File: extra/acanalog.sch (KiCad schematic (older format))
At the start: 20 parts, among them U1 TL074

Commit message: a lot more layout work
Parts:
- R10, R11, R12, R13, R14, R15, R16, R17, R18, R19, R20, R5, R6, R7, R8, R9: renamed from R?; footprint (none) -> xnorman:Resistor_Horizontal_RM10mm-xnorman
- gave numbers to parts that had none: 3
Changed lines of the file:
@@
 $EndDescr
 $Comp
-L CONN_01X03 P?
+L CONN_01X03 P7
 U 1 1 58575363
 P 1200 1350
-F 0 "P?" H 1200 1550 50  0000 C CNN
+F 0 "P7" H 1200 1550 50  0000 C CNN
 F 1 "CONN_01X03" V 1300 1350 50  0000 C CNN
-F 2 "" H 1200 1350 50  0000 C CNN
+F 2 "" H 1200 1350 50  0001 C CNN
 F 3 "" H 1200 1350 50  0000 C CNN
 	1    1200 1350
@@
 $EndComp
 $Comp
-L CONN_01X03 P?
+L CONN_01X03 P8
 U 1 1 5857536A
 P 5100 1250
-F 0 "P?" H 5100 1450 50  0000 C CNN
+F 0 "P8" H 5100 1450 50  0000 C CNN
 F 1 "CONN_01X03" V 5200 1250 50  0000 C CNN
-F 2 "" H 5100 1250 50  0000 C CNN
+F 2 "" H 5100 1250 50  0001 C CNN
 F 3 "" H 5100 1250 50  0000 C CNN
 	1    5100 1250
@@
 F 0 "U1" H 3000 2150 50  0000 C CNN
 F 1 "TL074" H 3100 1750 50  0000 C CNN
-F 2 "" H 2900 2050 50  0000 C CNN
+F 2 "" H 2900 2050 50  0001 C CNN
 F 3 "" H 3000 2150 50  0000 C CNN
 	1    2950 1950
@@
 $EndComp
 $Comp
-L R R?
+L R R5
 U 1 1 58575378
 P 2000 2050
-F 0 "R?" V 2080 2050 50  0000 C CNN
+F 0 "R5" V 2080 2050 50  0000 C CNN
 F 1 "2k" V 2000 2050 50  0000 C CNN
-F 2 "" V 1930 2050 50  0000 C CNN
+F 2 "xnorman:Resistor_Horizontal_RM10mm-xnorman" V 1930 2050 50  0001 C CNN
 F 3 "" H 2000 2050 50  0000 C CNN
 	1    2000 2050
@@
 $EndComp
 $Comp
-L R R?
+L R R9
 U 1 1 5857537F
 P 3050 2600
-F 0 "R?" V 3130 2600 50  0000 C CNN
+F 0 "R9" V 3130 2600 50  0000 C CNN
 F 1 "10k" V 3050 2600 50  0000 C CNN
-F 2 "" V 2980 2600 50  0000 C CNN
+F 2 "xnorman:Resistor_Horizontal_RM10mm-xnorman" V 2980 2600 50  0001 C CNN
 F 3 "" H 3050 2600 50  0000 C CNN
 	1    3050 2600
@@
 Connection ~ 2300 2050
 $Comp
-L GND #PWR?
+L GND #PWR08
 U 1 1 5857538D
 P 2450 1750
-F 0 "#PWR?" H 2450 1500 50  0001 C CNN
+F 0 "#PWR08" H 2450 1500 50  0001 C CNN
 F 1 "GND" H 2450 1600 50  0000 C CNN
 F 2 "" H 2450 1750 50  0000 C CNN
@@
 Connection ~ 3450 1950
 $Comp
-L R R?
+L R R13
 U 1 1 5857539F
 P 3700 1950
-F 0 "R?" V 3780 1950 50  0000 C CNN
+F 0 "R13" V 3780 1950 50  0000 C CNN
 F 1 "1k" V 3700 1950 50  0000 C CNN
-F 2 "" V 3630 1950 50  0000 C CNN
+F 2 "xnorman:Resistor_Horizontal_RM10mm-xnorman" V 3630 1950 50  0001 C CNN
 F 3 "" H 3700 1950 50  0000 C CNN
 	1    3700 1950
@@
 F 0 "U1" H 3000 3500 50  0000 C CNN
 F 1 "TL074" H 3100 3100 50  0000 C CNN
-F 2 "" H 2900 3400 50  0000 C CNN
+F 2 "" H 2900 3400 50  0001 C CNN
 F 3 "" H 3000 3500 50  0000 C CNN
 	2    2950 3300
@@
 $EndComp
 $Comp
-L R R?
+L R R6
 U 1 1 585753AE
 P 2000 3400
-F 0 "R?" V 2080 3400 50  0000 C CNN
+F 0 "R6" V 2080 3400 50  0000 C CNN
 F 1 "2k" V 2000 3400 50  0000 C CNN
-F 2 "" V 1930 3400 50  0000 C CNN
+F 2 "xnorman:Resistor_Horizontal_RM10mm-xnorman" V 1930 3400 50  0001 C CNN
 F 3 "" H 2000 3400 50  0000 C CNN
 	1    2000 3400
@@
 $EndComp
 $Comp
-L R R?
+L R R10
 U 1 1 585753B5
 P 3050 3950
-F 0 "R?" V 3130 3950 50  0000 C CNN
+F 0 "R10" V 3130 3950 50  0000 C CNN
 F 1 "10k" V 3050 3950 50  0000 C CNN
-F 2 "" V 2980 3950 50  0000 C CNN
+F 2 "xnorman:Resistor_Horizontal_RM10mm-xnorman" V 2980 3950 50  0001 C CNN
 F 3 "" H 3050 3950 50  0000 C CNN
 	1    3050 3950
@@
 Connection ~ 2300 3400
 $Comp
-L GND #PWR?
+L GND #PWR09
 U 1 1 585753C3
 P 2450 3100
-F 0 "#PWR?" H 2450 2850 50  0001 C CNN
+F 0 "#PWR09" H 2450 2850 50  0001 C CNN
 F 1 "GND" H 2450 2950 50  0000 C CNN
 F 2 "" H 2450 3100 50  0000 C CNN
@@
 Connection ~ 3450 3300
 $Comp
-L R R?
+L R R14
 U 1 1 585753D5
 P 3700 3300
-F 0 "R?" V 3780 3300 50  0000 C CNN
+F 0 "R14" V 3780 3300 50  0000 C CNN
 F 1 "1k" V 3700 3300 50  0000 C CNN
-F 2 "" V 3630 3300 50  0000 C CNN
+F 2 "xnorman:Resistor_Horizontal_RM10mm-xnorman" V 3630 3300 50  0001 C CNN
 F 3 "" H 3700 3300 50  0000 C CNN
 	1    3700 3300
@@
 F 0 "U1" H 3000 4950 50  0000 C CNN
 F 1 "TL074" H 3100 4550 50  0000 C CNN
-F 2 "" H 2900 4850 50  0000 C CNN
+F 2 "" H 2900 4850 50  0001 C CNN
 F 3 "" H 3000 4950 50  0000 C CNN
 	4    2950 4750
@@
 $EndComp
 $Comp
-L R R?
+L R R7
 U 1 1 585753E4
 P 2000 4850
-F 0 "R?" V 2080 4850 50  0000 C CNN
+F 0 "R7" V 2080 4850 50  0000 C CNN
 F 1 "100k" V 2000 4850 50  0000 C CNN
-F 2 "" V 1930 4850 50  0000 C CNN
+F 2 "xnorman:Resistor_Horizontal_RM10mm-xnorman" V 1930 4850 50  0001 C CNN
 F 3 "" H 2000 4850 50  0000 C CNN
 	1    2000 4850
@@
 $EndComp
 $Comp
-L R R?
+L R R11
 U 1 1 585753EB
 P 3050 5400
-F 0 "R?" V 3130 5400 50  0000 C CNN
+F 0 "R11" V 3130 5400 50  0000 C CNN
 F 1 "100k" V 3050 5400 50  0000 C CNN
-F 2 "" V 2980 5400 50  0000 C CNN
+F 2 "xnorman:Resistor_Horizontal_RM10mm-xnorman" V 2980 5400 50  0001 C CNN
 F 3 "" H 3050 5400 50  0000 C CNN
 	1    3050 5400
@@
 Connection ~ 2300 4850
 $Comp
-L GND #PWR?
+L GND #PWR010
 U 1 1 585753F9
 P 2450 4550
-F 0 "#PWR?" H 2450 4300 50  0001 C CNN
+F 0 "#PWR010" H 2450 4300 50  0001 C CNN
 F 1 "GND" H 2450 4400 50  0000 C CNN
 F 2 "" H 2450 4550 50  0000 C CNN
@@
 Connection ~ 3450 4750
 $Comp
-L R R?
+L R R15
 U 1 1 5857540B
 P 3700 4750
-F 0 "R?" V 3780 4750 50  0000 C CNN
+F 0 "R15" V 3780 4750 50  0000 C CNN
 F 1 "2k" V 3700 4750 50  0000 C CNN
-F 2 "" V 3630 4750 50  0000 C CNN
+F 2 "xnorman:Resistor_Horizontal_RM10mm-xnorman" V 3630 4750 50  0001 C CNN
 F 3 "" H 3700 4750 50  0000 C CNN
 	1    3700 4750
@@
 $EndComp
 $Comp
-L R R?
+L R R17
 U 1 1 58575412
 P 4100 4750
-F 0 "R?" V 4180 4750 50  0000 C CNN
+F 0 "R17" V 4180 4750 50  0000 C CNN
 F 1 "2k" V 4100 4750 50  0000 C CNN
-F 2 "" V 4030 4750 50  0000 C CNN
+F 2 "xnorman:Resistor_Horizontal_RM10mm-xnorman" V 4030 4750 50  0001 C CNN
 F 3 "" H 4100 4750 50  0000 C CNN
 	1    4100 4750
@@
 $EndComp
 $Comp
-L R R?
+L R R19
 U 1 1 58575419
 P 4400 5000
-F 0 "R?" V 4480 5000 50  0000 C CNN
+F 0 "R19" V 4480 5000 50  0000 C CNN
 F 1 "1k" V 4400 5000 50  0000 C CNN
-F 2 "" V 4330 5000 50  0000 C CNN
+F 2 "xnorman:Resistor_Horizontal_RM10mm-xnorman" V 4330 5000 50  0001 C CNN
 F 3 "" H 4400 5000 50  0000 C CNN
 	1    4400 5000
@@
 Connection ~ 4400 4750
 $Comp
-L GND #PWR?
+L GND #PWR011
 U 1 1 58575424
 P 4400 5300
-F 0 "#PWR?" H 4400 5050 50  0001 C CNN
+F 0 "#PWR011" H 4400 5050 50  0001 C CNN
 F 1 "GND" H 4400 5150 50  0000 C CNN
 F 2 "" H 4400 5300 50  0000 C CNN
@@
 F 0 "U1" H 3000 6300 50  0000 C CNN
 F 1 "TL074" H 3100 5900 50  0000 C CNN
-F 2 "" H 2900 6200 50  0000 C CNN
+F 2 "" H 2900 6200 50  0001 C CNN
 F 3 "" H 3000 6300 50  0000 C CNN
 	3    2950 6100
@@
 $EndComp
 $Comp
-L R R?
+L R R8
 U 1 1 58575432
 P 2000 6200
-F 0 "R?" V 2080 6200 50  0000 C CNN
+F 0 "R8" V 2080 6200 50  0000 C CNN
 F 1 "100k" V 2000 6200 50  0000 C CNN
-F 2 "" V 1930 6200 50  0000 C CNN
+F 2 "xnorman:Resistor_Horizontal_RM10mm-xnorman" V 1930 6200 50  0001 C CNN
 F 3 "" H 2000 6200 50  0000 C CNN
 	1    2000 6200
@@
 $EndComp
 $Comp
-L R R?
+L R R12
 U 1 1 58575439
 P 3050 6750
-F 0 "R?" V 3130 6750 50  0000 C CNN
+F 0 "R12" V 3130 6750 50  0000 C CNN
 F 1 "100k" V 3050 6750 50  0000 C CNN
-F 2 "" V 2980 6750 50  0000 C CNN
+F 2 "xnorman:Resistor_Horizontal_RM10mm-xnorman" V 2980 6750 50  0001 C CNN
 F 3 "" H 3050 6750 50  0000 C CNN
 	1    3050 6750
@@
 Connection ~ 2300 6200
 $Comp
-L GND #PWR?
+L GND #PWR012
 U 1 1 58575447
 P 2450 5900
-F 0 "#PWR?" H 2450 5650 50  0001 C CNN
+F 0 "#PWR012" H 2450 5650 50  0001 C CNN
 F 1 "GND" H 2450 5750 50  0000 C CNN
 F 2 "" H 2450 5900 50  0000 C CNN
@@
 Connection ~ 3450 6100
 $Comp
-L R R?
+L R R16
 U 1 1 58575459
 P 3700 6100
-F 0 "R?" V 3780 6100 50  0000 C CNN
+F 0 "R16" V 3780 6100 50  0000 C CNN
 F 1 "2k" V 3700 6100 50  0000 C CNN
-F 2 "" V 3630 6100 50  0000 C CNN
+F 2 "xnorman:Resistor_Horizontal_RM10mm-xnorman" V 3630 6100 50  0001 C CNN
 F 3 "" H 3700 6100 50  0000 C CNN
 	1    3700 6100
@@
 $EndComp
 $Comp
-L R R?
+L R R18
 U 1 1 58575460
 P 4100 6100
-F 0 "R?" V 4180 6100 50  0000 C CNN
+F 0 "R18" V 4180 6100 50  0000 C CNN
 F 1 "2k" V 4100 6100 50  0000 C CNN
-F 2 "" V 4030 6100 50  0000 C CNN
+F 2 "xnorman:Resistor_Horizontal_RM10mm-xnorman" V 4030 6100 50  0001 C CNN
 F 3 "" H 4100 6100 50  0000 C CNN
 	1    4100 6100
@@
 $EndComp
 $Comp
-L R R?
+L R R20
 U 1 1 58575467
 P 4400 6350
-F 0 "R?" V 4480 6350 50  0000 C CNN
+F 0 "R20" V 4480 6350 50  0000 C CNN
 F 1 "1k" V 4400 6350 50  0000 C CNN
-F 2 "" V 4330 6350 50  0000 C CNN
+F 2 "xnorman:Resistor_Horizontal_RM10mm-xnorman" V 4330 6350 50  0001 C CNN
 F 3 "" H 4400 6350 50  0000 C CNN
 	1    4400 6350
@@
 Connection ~ 4400 6100
 $Comp
-L GND #PWR?
+L GND #PWR013
 U 1 1 58575472
 P 4400 6650
-F 0 "#PWR?" H 4400 6400 50  0001 C CNN
+F 0 "#PWR013" H 4400 6400 50  0001 C CNN
 F 1 "GND" H 4400 6500 50  0000 C CNN
 F 2 "" H 4400 6650 50  0000 C CNN
@@
 	1450 1350 1400 1350
 $Comp
-L GND #PWR?
+L GND #PWR014
 U 1 1 58575BEC
 P 1550 1550
-F 0 "#PWR?" H 1550 1300 50  0001 C CNN
+F 0 "#PWR014" H 1550 1300 50  0001 C CNN
 F 1 "GND" H 1550 1400 50  0000 C CNN
 F 2 "" H 1550 1550 50  0000 C CNN
@@
 belaacin2
 $Comp
-L GND #PWR?
+L GND #PWR015
 U 1 1 58575F21
 P 4700 1450
-F 0 "#PWR?" H 4700 1200 50  0001 C CNN
+F 0 "#PWR015" H 4700 1200 50  0001 C CNN
 F 1 "GND" H 4700 1300 50  0000 C CNN
 F 2 "" H 4700 1450 50  0000 C CNN
@@
 	4700 1350 4700 1450
 $Comp
-L CONN_02X04 P?
+L CONN_02X04 P9
 U 1 1 585765EB
 P 6650 3100
-F 0 "P?" H 6650 3350 50  0000 C CNN
+F 0 "P9" H 6650 3350 50  0000 C CNN
 F 1 "mod_ac-io" H 6650 2850 50  0000 C CNN
-F 2 "" H 6650 1900 50  0000 C CNN
+F 2 "" H 6650 1900 50  0001 C CNN
 F 3 "" H 6650 1900 50  0000 C CNN
 	1    6650 3100
@@
 	6350 3350 6150 3350
 $Comp
-L GND #PWR?
+L GND #PWR016
 U 1 1 58576B81
 P 6900 3400
-F 0 "#PWR?" H 6900 3150 50  0001 C CNN
+F 0 "#PWR016" H 6900 3150 50  0001 C CNN
 F 1 "GND" H 6900 3250 50  0000 C CNN
 F 2 "" H 6900 3400 50  0000 C CNN

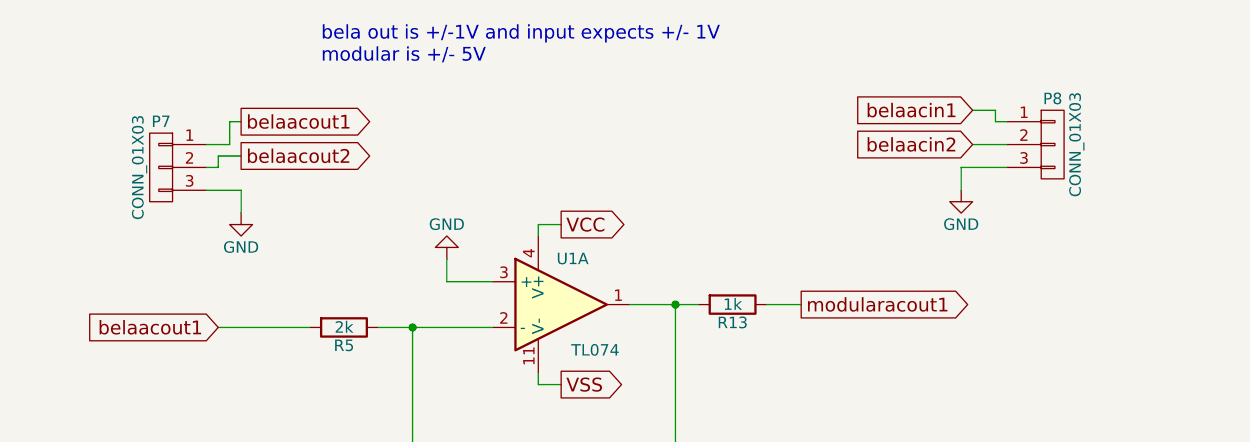
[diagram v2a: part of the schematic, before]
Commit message: starting pcb layout a little
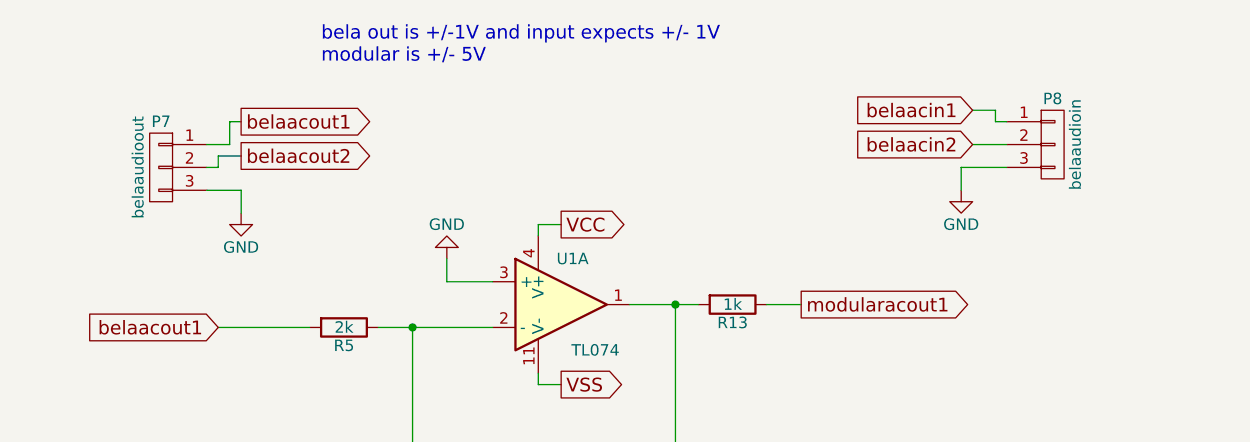
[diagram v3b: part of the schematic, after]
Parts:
- P7: value CONN_01X03 -> belaaudioout; footprint (none) -> Pin_Headers:Pin_Header_Straight_1x03_Pitch2.54mm
- P8: value CONN_01X03 -> belaaudioin; footprint (none) -> Pin_Headers:Pin_Header_Straight_1x03_Pitch2.54mm
- P9: footprint (none) -> Pin_Headers:Pin_Header_Straight_2x04_Pitch2.54mm
- U1: footprint (none) -> Housings_DIP:DIP-14_W7.62mm_LongPads
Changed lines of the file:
@@
 P 1200 1350
 F 0 "P7" H 1200 1550 50  0000 C CNN
-F 1 "CONN_01X03" V 1300 1350 50  0000 C CNN
-F 2 "" H 1200 1350 50  0001 C CNN
+F 1 "belaaudioout" V 1300 1350 50  0000 C CNN
+F 2 "Pin_Headers:Pin_Header_Straight_1x03_Pitch2.54mm" H 1200 1350 50  0001 C CNN
 F 3 "" H 1200 1350 50  0000 C CNN
 	1    1200 1350
@@
 P 5100 1250
 F 0 "P8" H 5100 1450 50  0000 C CNN
-F 1 "CONN_01X03" V 5200 1250 50  0000 C CNN
-F 2 "" H 5100 1250 50  0001 C CNN
+F 1 "belaaudioin" V 5200 1250 50  0000 C CNN
+F 2 "Pin_Headers:Pin_Header_Straight_1x03_Pitch2.54mm" H 5100 1250 50  0001 C CNN
 F 3 "" H 5100 1250 50  0000 C CNN
 	1    5100 1250
@@
 F 0 "U1" H 3000 2150 50  0000 C CNN
 F 1 "TL074" H 3100 1750 50  0000 C CNN
-F 2 "" H 2900 2050 50  0001 C CNN
+F 2 "Housings_DIP:DIP-14_W7.62mm_LongPads" H 2900 2050 50  0001 C CNN
 F 3 "" H 3000 2150 50  0000 C CNN
 	1    2950 1950
@@
 F 0 "U1" H 3000 3500 50  0000 C CNN
 F 1 "TL074" H 3100 3100 50  0000 C CNN
-F 2 "" H 2900 3400 50  0001 C CNN
+F 2 "Housings_DIP:DIP-14_W7.62mm_LongPads" H 2900 3400 50  0001 C CNN
 F 3 "" H 3000 3500 50  0000 C CNN
 	2    2950 3300
@@
 F 0 "U1" H 3000 4950 50  0000 C CNN
 F 1 "TL074" H 3100 4550 50  0000 C CNN
-F 2 "" H 2900 4850 50  0001 C CNN
+F 2 "Housings_DIP:DIP-14_W7.62mm_LongPads" H 2900 4850 50  0001 C CNN
 F 3 "" H 3000 4950 50  0000 C CNN
 	4    2950 4750
@@
 F 0 "U1" H 3000 6300 50  0000 C CNN
 F 1 "TL074" H 3100 5900 50  0000 C CNN
-F 2 "" H 2900 6200 50  0001 C CNN
+F 2 "Housings_DIP:DIP-14_W7.62mm_LongPads" H 2900 6200 50  0001 C CNN
 F 3 "" H 3000 6300 50  0000 C CNN
 	3    2950 6100
@@
 F 0 "P9" H 6650 3350 50  0000 C CNN
 F 1 "mod_ac-io" H 6650 2850 50  0000 C CNN
-F 2 "" H 6650 1900 50  0001 C CNN
+F 2 "Pin_Headers:Pin_Header_Straight_2x04_Pitch2.54mm" H 6650 1900 50  0001 C CNN
 F 3 "" H 6650 1900 50  0000 C CNN
 	1    6650 3100

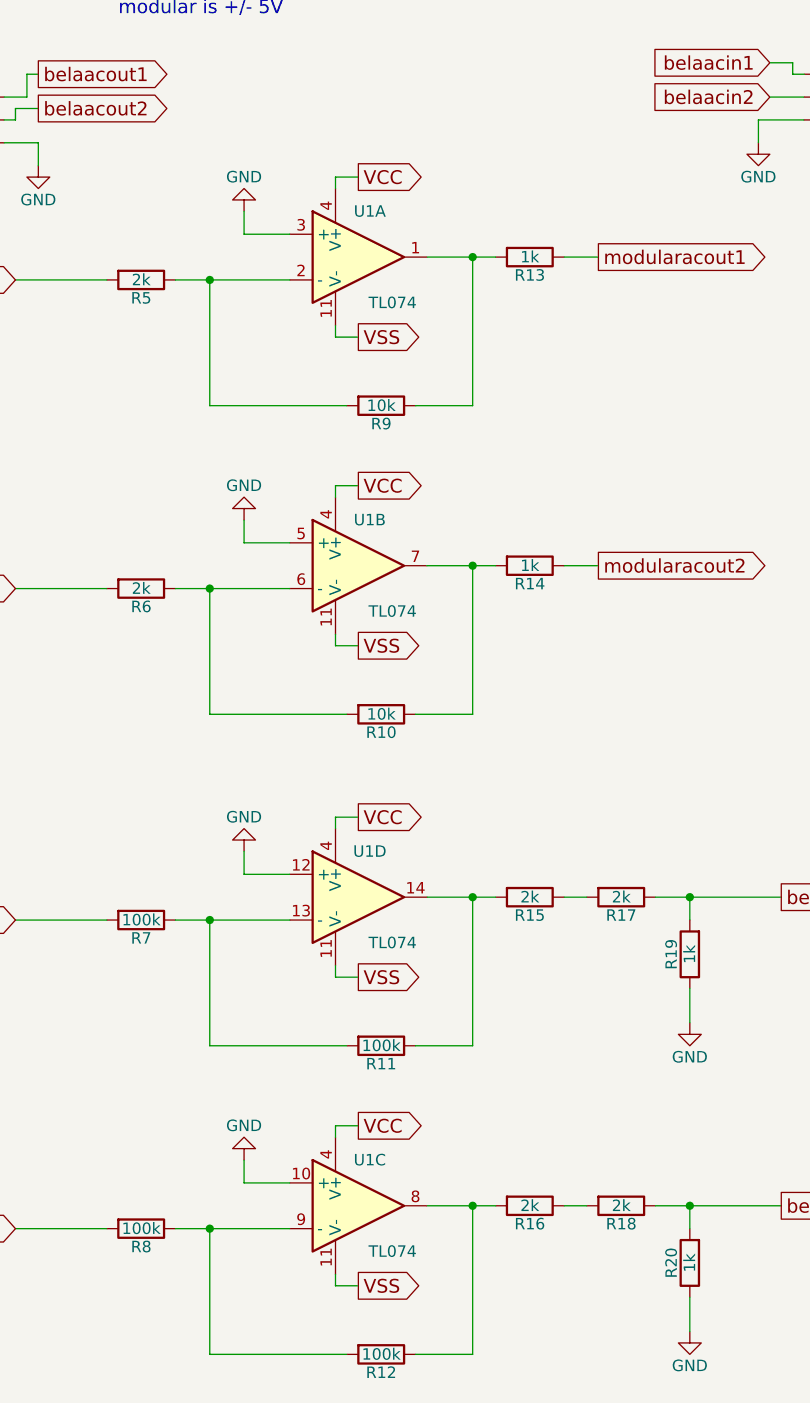
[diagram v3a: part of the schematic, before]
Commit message: moving along, still no idea why 5v is hooked to 3.3v
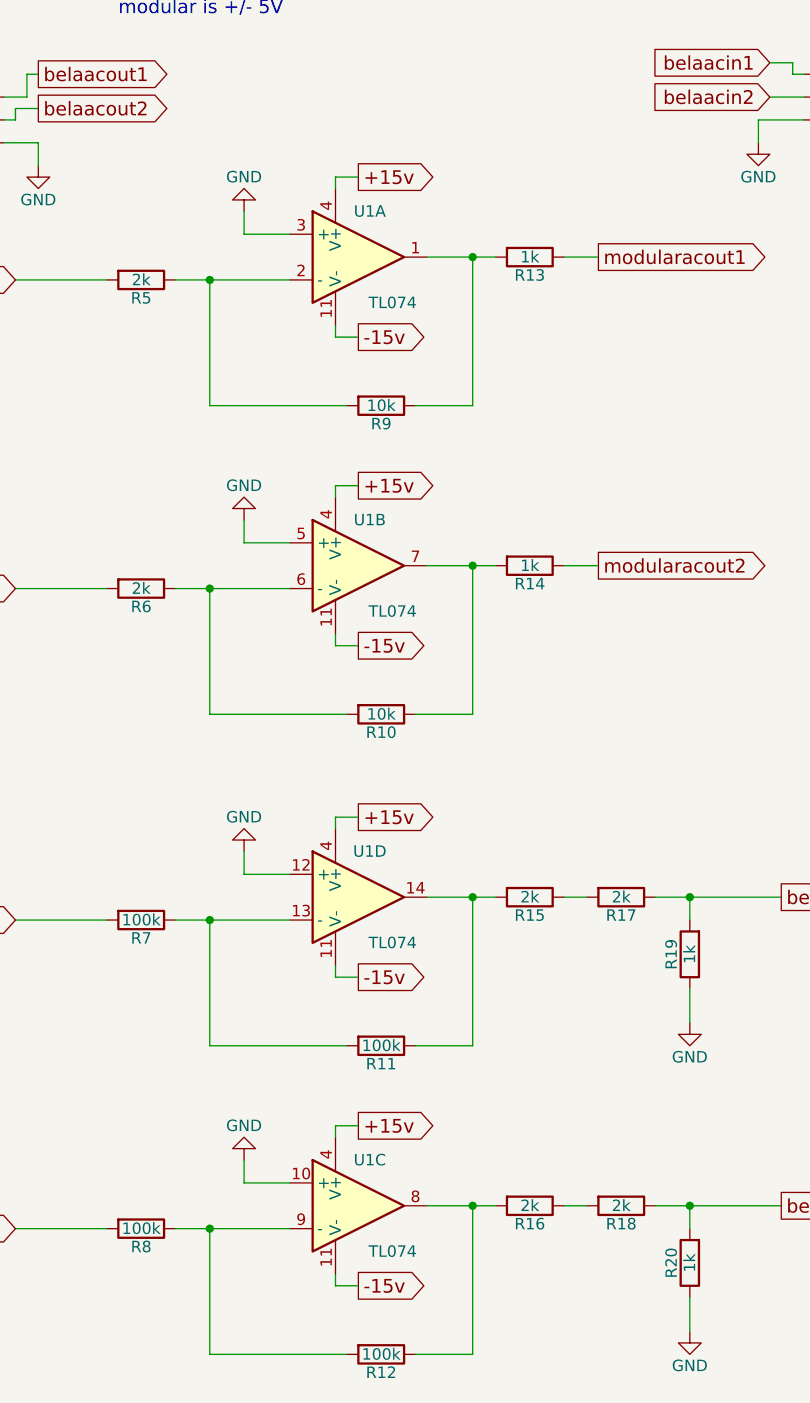
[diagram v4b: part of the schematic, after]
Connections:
- net VCC renamed +15v
- net VSS renamed -15v
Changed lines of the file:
@@
 LIBS:contrib
 LIBS:valves
+LIBS:xnorman
 LIBS:bela-extra-cache
 EELAYER 25 0
@@
 Connection ~ 2300 2050
 $Comp
-L GND #PWR08
+L GND #PWR09
 U 1 1 5857538D
 P 2450 1750
-F 0 "#PWR08" H 2450 1500 50  0001 C CNN
+F 0 "#PWR09" H 2450 1500 50  0001 C CNN
 F 1 "GND" H 2450 1600 50  0000 C CNN
 F 2 "" H 2450 1750 50  0000 C CNN
@@
 	2450 1850 2450 1750
 Text GLabel 2950 1600 2    60   Output ~ 0
-VCC
++15v
 Text GLabel 2950 2300 2    60   Output ~ 0
-VSS
+-15v
 Wire Wire Line
 	2850 2250 2850 2300
@@
 Connection ~ 2300 3400
 $Comp
-L GND #PWR09
+L GND #PWR010
 U 1 1 585753C3
 P 2450 3100
-F 0 "#PWR09" H 2450 2850 50  0001 C CNN
+F 0 "#PWR010" H 2450 2850 50  0001 C CNN
 F 1 "GND" H 2450 2950 50  0000 C CNN
 F 2 "" H 2450 3100 50  0000 C CNN
@@
 	2450 3200 2450 3100
 Text GLabel 2950 2950 2    60   Output ~ 0
-VCC
++15v
 Text GLabel 2950 3650 2    60   Output ~ 0
-VSS
+-15v
 Wire Wire Line
 	2850 3600 2850 3650
@@
 Connection ~ 2300 4850
 $Comp
-L GND #PWR010
+L GND #PWR011
 U 1 1 585753F9
 P 2450 4550
-F 0 "#PWR010" H 2450 4300 50  0001 C CNN
+F 0 "#PWR011" H 2450 4300 50  0001 C CNN
 F 1 "GND" H 2450 4400 50  0000 C CNN
 F 2 "" H 2450 4550 50  0000 C CNN
@@
 	2450 4650 2450 4550
 Text GLabel 2950 4400 2    60   Output ~ 0
-VCC
++15v
 Text GLabel 2950 5100 2    60   Output ~ 0
-VSS
+-15v
 Wire Wire Line
 	2850 5050 2850 5100
@@
 Connection ~ 4400 4750
 $Comp
-L GND #PWR011
+L GND #PWR012
 U 1 1 58575424
 P 4400 5300
-F 0 "#PWR011" H 4400 5050 50  0001 C CNN
+F 0 "#PWR012" H 4400 5050 50  0001 C CNN
 F 1 "GND" H 4400 5150 50  0000 C CNN
 F 2 "" H 4400 5300 50  0000 C CNN
@@
 Connection ~ 2300 6200
 $Comp
-L GND #PWR012
+L GND #PWR013
 U 1 1 58575447
 P 2450 5900
-F 0 "#PWR012" H 2450 5650 50  0001 C CNN
+F 0 "#PWR013" H 2450 5650 50  0001 C CNN
 F 1 "GND" H 2450 5750 50  0000 C CNN
 F 2 "" H 2450 5900 50  0000 C CNN
@@
 	2450 6000 2450 5900
 Text GLabel 2950 5750 2    60   Output ~ 0
-VCC
++15v
 Text GLabel 2950 6450 2    60   Output ~ 0
-VSS
+-15v
 Wire Wire Line
 	2850 6400 2850 6450
@@
 Connection ~ 4400 6100
 $Comp
-L GND #PWR013
+L GND #PWR014
 U 1 1 58575472
 P 4400 6650
-F 0 "#PWR013" H 4400 6400 50  0001 C CNN
+F 0 "#PWR014" H 4400 6400 50  0001 C CNN
 F 1 "GND" H 4400 6500 50  0000 C CNN
 F 2 "" H 4400 6650 50  0000 C CNN
@@
 	1450 1350 1400 1350
 $Comp
-L GND #PWR014
+L GND #PWR015
 U 1 1 58575BEC
 P 1550 1550
-F 0 "#PWR014" H 1550 1300 50  0001 C CNN
+F 0 "#PWR015" H 1550 1300 50  0001 C CNN
 F 1 "GND" H 1550 1400 50  0000 C CNN
 F 2 "" H 1550 1550 50  0000 C CNN
@@
 belaacin2
 $Comp
-L GND #PWR015
+L GND #PWR016
 U 1 1 58575F21
 P 4700 1450
-F 0 "#PWR015" H 4700 1200 50  0001 C CNN
+F 0 "#PWR016" H 4700 1200 50  0001 C CNN
 F 1 "GND" H 4700 1300 50  0000 C CNN
 F 2 "" H 4700 1450 50  0000 C CNN
@@
 	6350 3350 6150 3350
 $Comp
-L GND #PWR016
+L GND #PWR017
 U 1 1 58576B81
 P 6900 3400
-F 0 "#PWR016" H 6900 3150 50  0001 C CNN
+F 0 "#PWR017" H 6900 3150 50  0001 C CNN
 F 1 "GND" H 6900 3250 50  0000 C CNN
 F 2 "" H 6900 3400 50  0000 C CNN
